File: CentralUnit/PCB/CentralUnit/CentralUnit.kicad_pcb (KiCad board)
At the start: 2 copper layers, 10 parts, among them J1 Conn_02x20_Odd_Even, J2 Conn_01x06, J3 Conn_01x03_Male

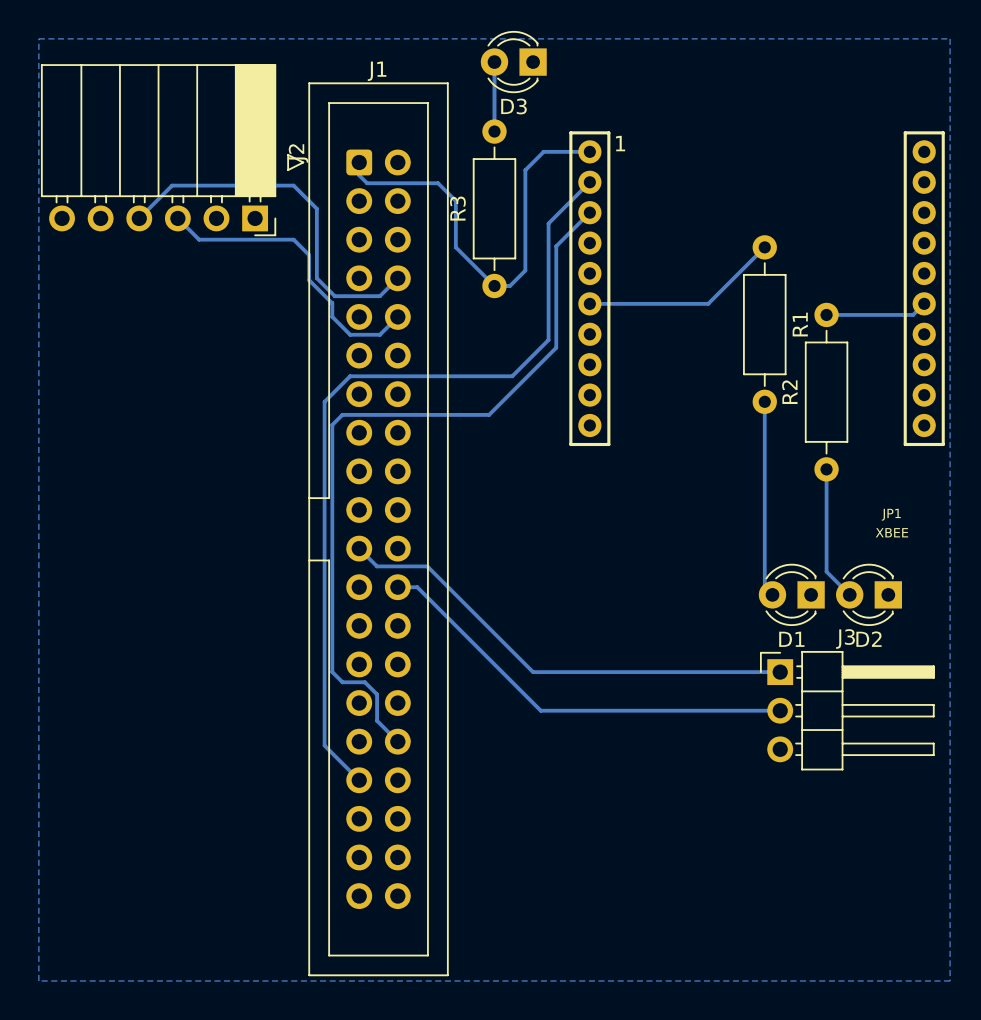
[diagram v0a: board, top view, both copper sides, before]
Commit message: Starting issue #29: Carrier PCB for central unit and improved PCBs for other units, as ordered.
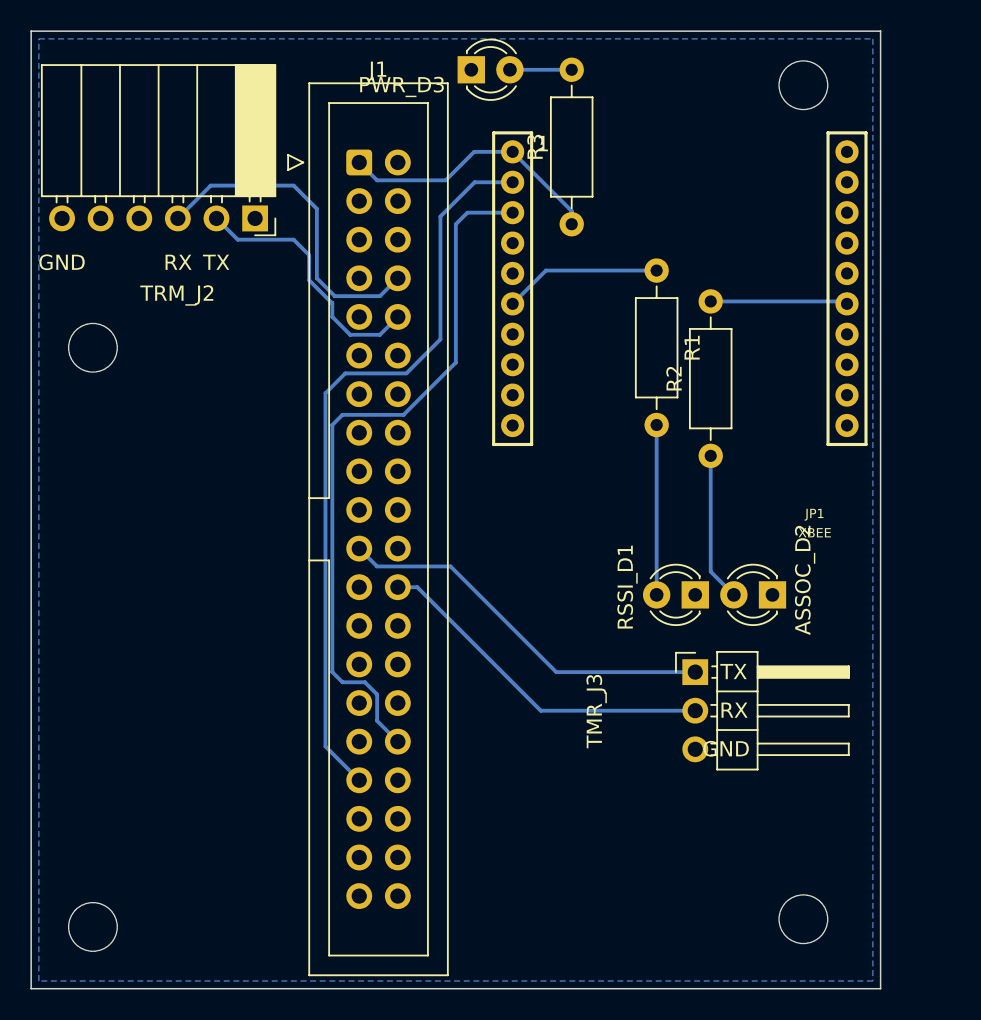
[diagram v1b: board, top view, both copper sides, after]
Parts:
- added H1: MountingHole, MountingHole:MountingHole_3.2mm_M3, F.Cu at (52.8, 42.2)
- added H2: MountingHole, MountingHole:MountingHole_3.2mm_M3, F.Cu at (52.8, 80.3)
- added H3: MountingHole, MountingHole:MountingHole_3.2mm_M3, F.Cu at (99.6, 24.9)
- added H4: MountingHole, MountingHole:MountingHole_3.2mm_M3, F.Cu at (99.6, 79.8)
- moved R2 7.67 mm to (93.5, 49.3)
- moved ASSOC_D2 7.62 mm to (97.5, 58.4)
- moved RSSI_D1 7.62 mm to (92.5, 58.4)
- moved R1 7.27 mm to (89.9, 37.1)
- moved R3 6.51 mm to (84.3, 34.0)
- moved TMR_J3 5.59 mm to (92.5, 63.5)
- moved JP1 5.08 mm to (91.4, 49.3)
- moved PWR_D3 4.10 mm to (77.7, 23.9), turned to 0 degrees
- renumbered D2 to ASSOC_D2, D3 to PWR_D3, D1 to RSSI_D1, J3 to TMR_J3, J2 to TRM_J2
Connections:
- TRM_J2 pad 2: Net-(J2-Pad2) -> TRM_TX
- TRM_J2 pad 3: TRM_TX -> TRM_RX
- TRM_J2 pad 4: TRM_RX -> Net-(TRM_J2-Pad4)
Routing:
- net +3V3: track 28.3 -> 17.7 mm
- net TMR_TX: track 31.1 -> 25.5 mm
- net TMR_RX: track 28.5 -> 22.9 mm
- net XBEE_TX: track 53.8 -> 49.2 mm
- net XBEE_RX: track 50.1 -> 46.5 mm
- net Net-(JP1-Pad6): track 13.0 -> 10.4 mm
- net TRM_TX: track 19.6 -> 17.1 mm
- net TRM_RX: track 24.1 -> 21.5 mm
- net Net-(JP1-Pad15): track 6.73 -> 9.03 mm
- net Net-(R1-Pad2): track 12.9 -> 11.2 mm
- net Net-(ASSOC_D2-Pad2): track 8.89 -> 9.78 mm
- net Net-(PWR_D3-Pad2): track 4.57 -> 4.06 mm
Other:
- board outline added: 55.9 x 63 mm
- board text added: "GND"
- board text added: "RX"
- board text added: "TX"
